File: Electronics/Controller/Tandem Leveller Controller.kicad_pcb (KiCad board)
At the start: 2 copper layers, 212 x 145 mm, 133 parts, among them J1 Conn_01x02, J10 CAN BUS, J11 TRACTOR BATTERY, J12 PWR SWITCH, J13 VALVE POWER, J14 TABLET 1 PWR, J15 TABLET 2 PWR, J16 SLAVE TABLET, J17 MASTER TABLET, J18 292303-7, J19 292303-7, J2 GPS SIM, J20 FRONT HEIGHT, J21 REAR HEIGHT, J23 CAN, J24 CAN BUS, J25 CAN BUS, J3 Conn_01x02, J4 Conn_01x02, J5 Conn_01x02, J6 Conn_01x02, J7 Conn_01x02, J8 Conn_01x02, J9 TERM, U1 TEENSY 4.0, U10 FT232RL, U11 FT232RL, U12 FT232RL, U13 FT232RL, U14 FT232RL, U15 FT232RL, U16 USB2517, U17 MIC2026-1YM, U2 simpleRTK2B, U3 simpleRTK2B, U4 simpleRTK2B, U5 TJA1462ATK-0Z, U6 PESD2CANFD24V-TR, U7 LM2596S-5, U8 LM2587S-ADJ/NOPB, U9 LM2587S-ADJ/NOPB, Y1 FA-238 24.0000MD30X-W5

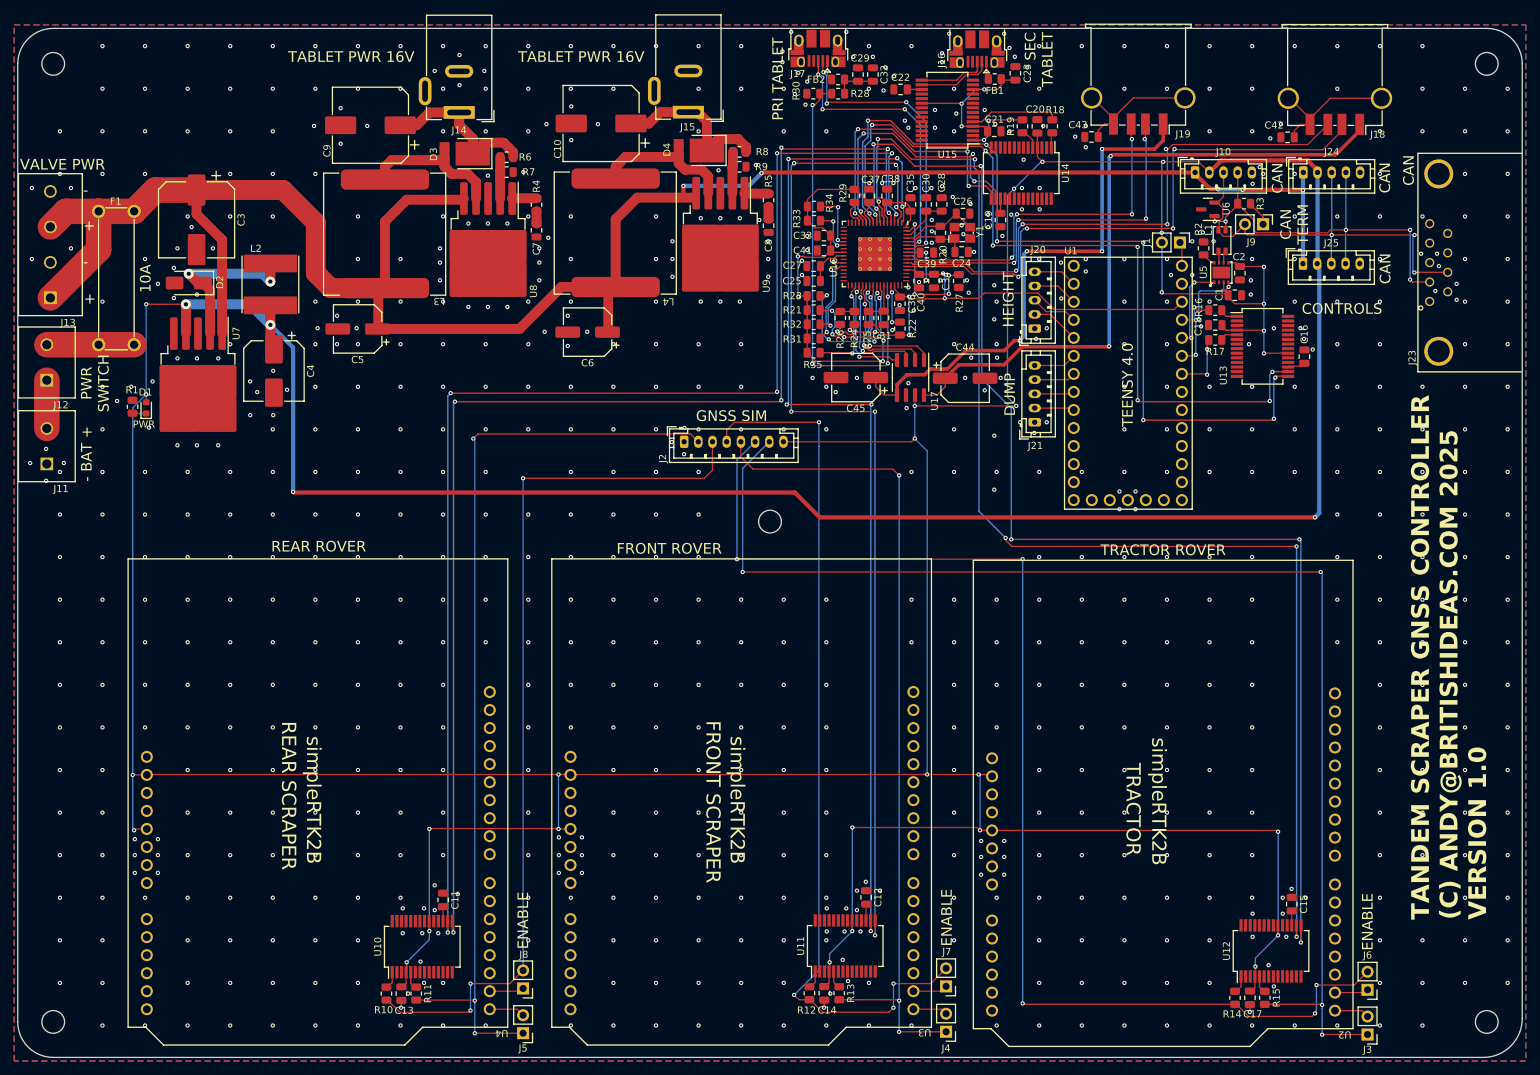
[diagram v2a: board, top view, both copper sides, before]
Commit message: Added 4.7uF caps to FT232RL on controller.
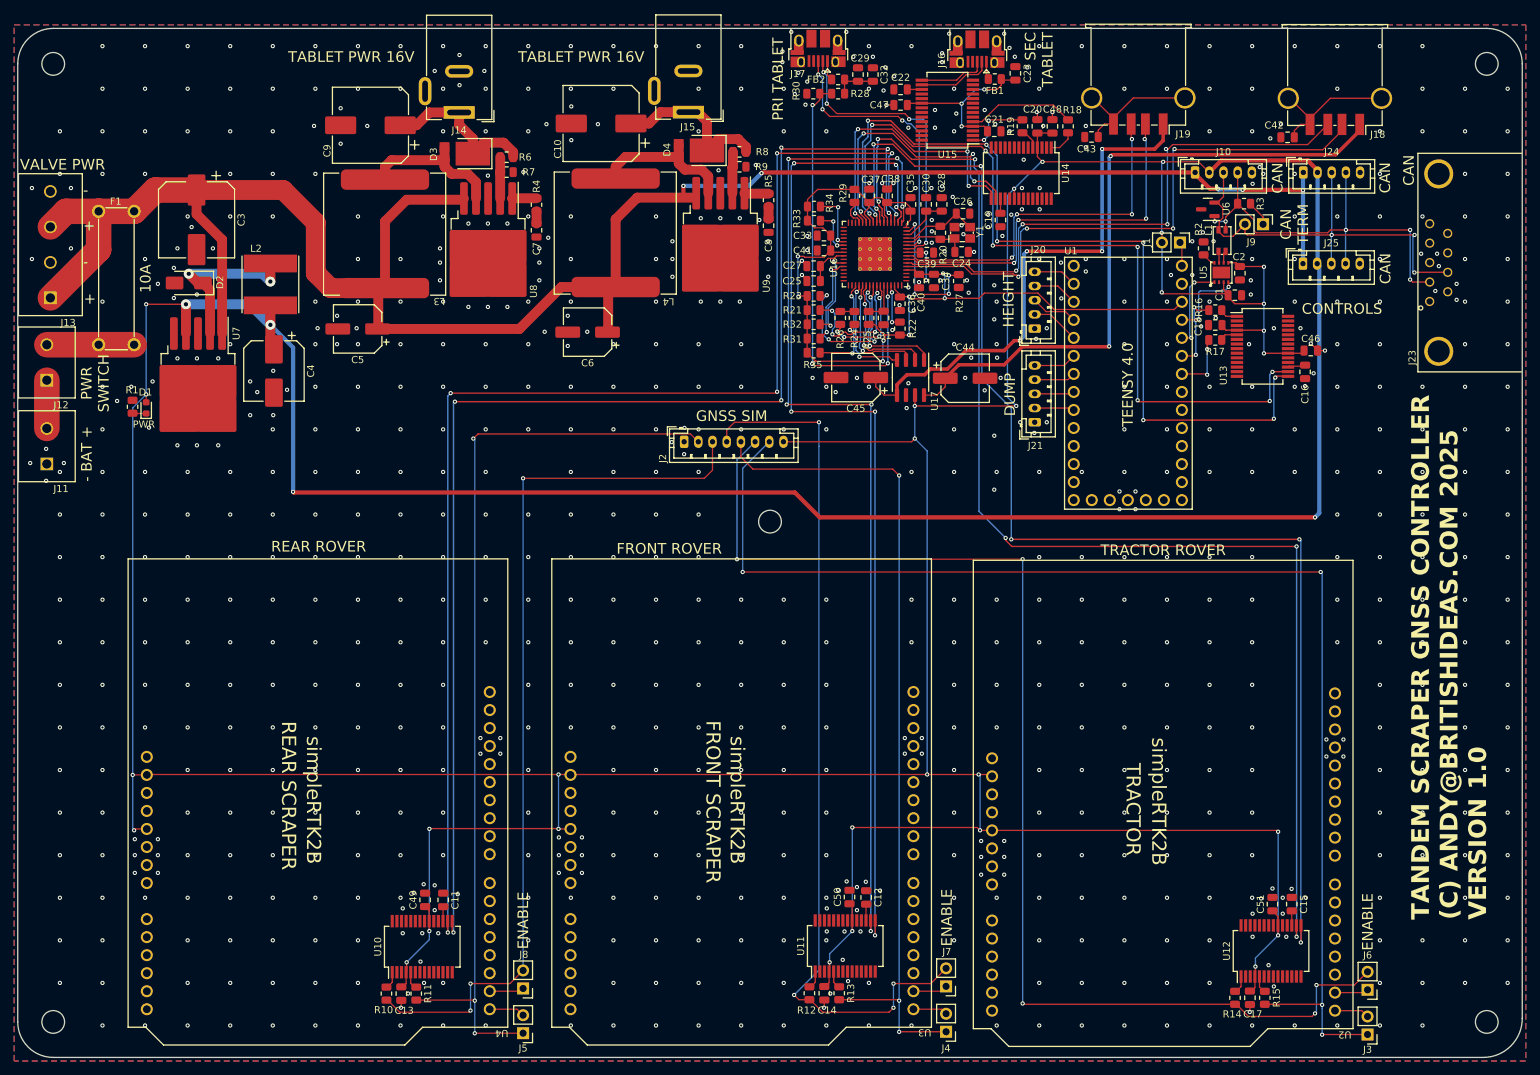
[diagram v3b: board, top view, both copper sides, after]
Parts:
- added C46: 4u7, Capacitor_SMD:C_0805_2012Metric, F.Cu at (236.2, 69.4)
- added C47: 4u7, Capacitor_SMD:C_0805_2012Metric, F.Cu at (178.4, 34.8)
- added C48: 4u7, Capacitor_SMD:C_0805_2012Metric, F.Cu at (199.8, 37.8)
- added C49: 4u7, Capacitor_SMD:C_0805_2012Metric, F.Cu at (111.4, 146.8)
- added C50: 4u7, Capacitor_SMD:C_0805_2012Metric, F.Cu at (171.2, 146.4)
- added C51: 4u7, Capacitor_SMD:C_0805_2012Metric, F.Cu at (230.8, 147.4)
- R1: value 287 -> 330
- R4, R5: value 2k94 -> 3k
- R6, R8: value 17k8 -> 18k
- moved R18 2.22 mm to (202.0, 37.8)
- moved C16 2.15 mm to (235.4, 72.4), turned to 90 degrees
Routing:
- net +5V: track 854.4 -> 866.0 mm
- net GND: track 9.72 -> 15.3 mm, vias 845 -> 865
- net Net-(U15-RXD): track 12.6 -> 15.2 mm
- net Net-(U15-VCC): track 22.5 -> 24.6 mm
- net Net-(U14-TXD): track 2.15 -> 3.76 mm
- net Net-(J17-D+): track 40.3 -> 39.5 mm
